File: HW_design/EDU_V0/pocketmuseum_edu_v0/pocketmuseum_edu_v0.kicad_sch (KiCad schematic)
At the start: 1 part

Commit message: Updated Readme
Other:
- note added: "ADD INTERRUPT PIN AT ESP32 ADD POWER SWITCH FIGURE OUT I2C ROUTING"
- company: (none) -> Bucharest Applied STEAM Museum
- title: BASM POCKETMUSEUM EDU V0 -> POCKETMUSEUM EDU V0
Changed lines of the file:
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@@
 	(paper "A4")
 	(title_block
-		(title "BASM POCKETMUSEUM EDU V0")
-		(date "2025-06-30")
+		(title "POCKETMUSEUM EDU V0")
+		(date "2025-08-01")
+		(company "Bucharest Applied STEAM Museum")
 	)
 	(rectangle
@@
 	(text "I2C  Bus Topology: ESP32 <> Pull-up Resistors <> ICP20100 (BARO) \n							<> Level Shifter <> Pull-up Resistors <> ICM20948 (9-Axis IMU)\nSPI Bus Topology: ESP32 <> Pull-up Resistors <> MicroSD Card\nWS2812B Bus Topology: ESP32 <> Data Line Resistor <> RGB LED #1 <> ... <> RGB LED #9"
 		(exclude_from_sim no)
-		(at 22.606 153.924 0)
+		(at 20.574 157.226 0)
 		(effects
 			(font
@@
 			)
 		)
+	)
+	(text "ADD INTERRUPT PIN AT ESP32\nADD POWER SWITCH\nFIGURE OUT I2C ROUTING"
+		(exclude_from_sim no)
+		(at 238.252 117.602 0)
+		(effects
+			(font
+				(size 3.048 3.048)
+				(color 255 54 93 1)
+			)
+		)

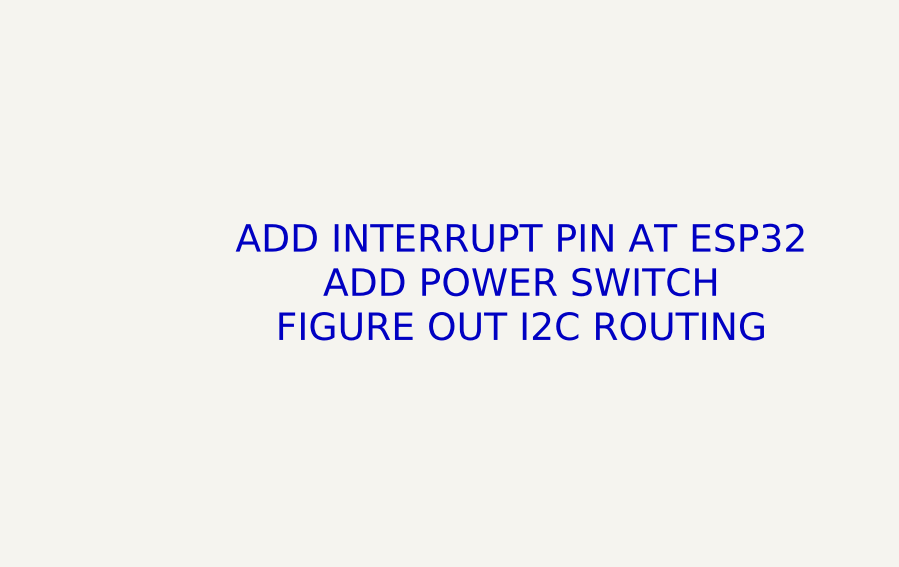
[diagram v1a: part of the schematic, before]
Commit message: Added Mic & Light Sensor to EDU_V0
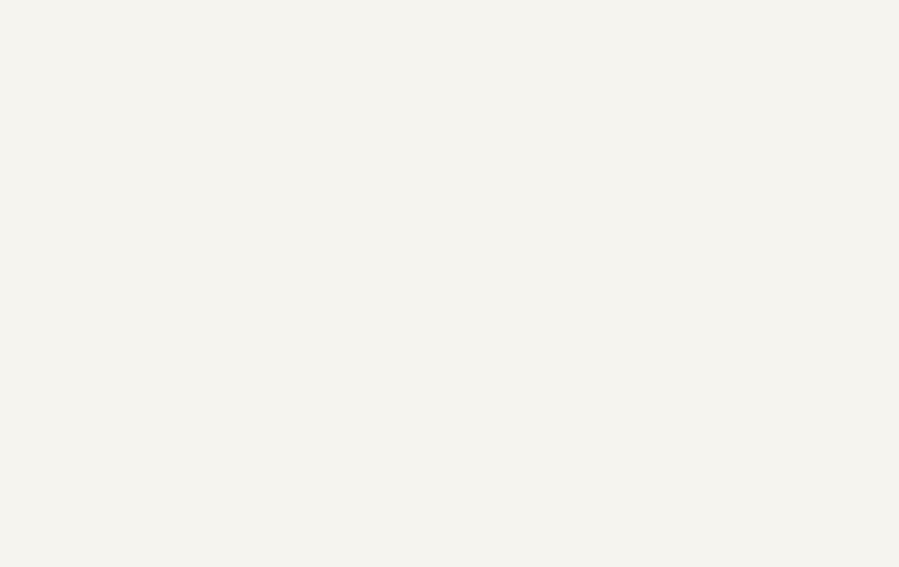
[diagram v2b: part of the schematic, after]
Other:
- note removed: "ADD INTERRUPT PIN AT ESP32 ADD POWER SWITCH FIGURE OUT I2C ROUTING"
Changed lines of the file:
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@@
 	(title_block
 		(title "POCKETMUSEUM EDU V0")
-		(date "2025-08-01")
+		(date "2025-08-18")
+		(rev "2")
 		(company "Bucharest Applied STEAM Museum")
 	)
@@
 			)
 		)
-	)
-	(text "ADD INTERRUPT PIN AT ESP32\nADD POWER SWITCH\nFIGURE OUT I2C ROUTING"
-		(exclude_from_sim no)
-		(at 238.252 117.602 0)
-		(effects
-			(font
-				(size 3.048 3.048)
-				(color 255 54 93 1)
-			)
-		)

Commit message: EDUV0 HW Complete Placement
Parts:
- added H2, H3, H4: MountingHole, MountingHole:MountingHole_3.2mm_M3, symbol Mechanical:MountingHole
- H1: footprint MountingHole:MountingHole_3.5mm -> MountingHole:MountingHole_3.2mm_M3
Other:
- moved on the sheet: H1
